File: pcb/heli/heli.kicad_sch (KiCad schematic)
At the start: 18 parts, among them J1 Batterie, J2 Debug, J3 Radio, Q1 IRLZ44N, SW1 SW_Push, U1 AZ1117-3.3, U2 STM32F103CBTx

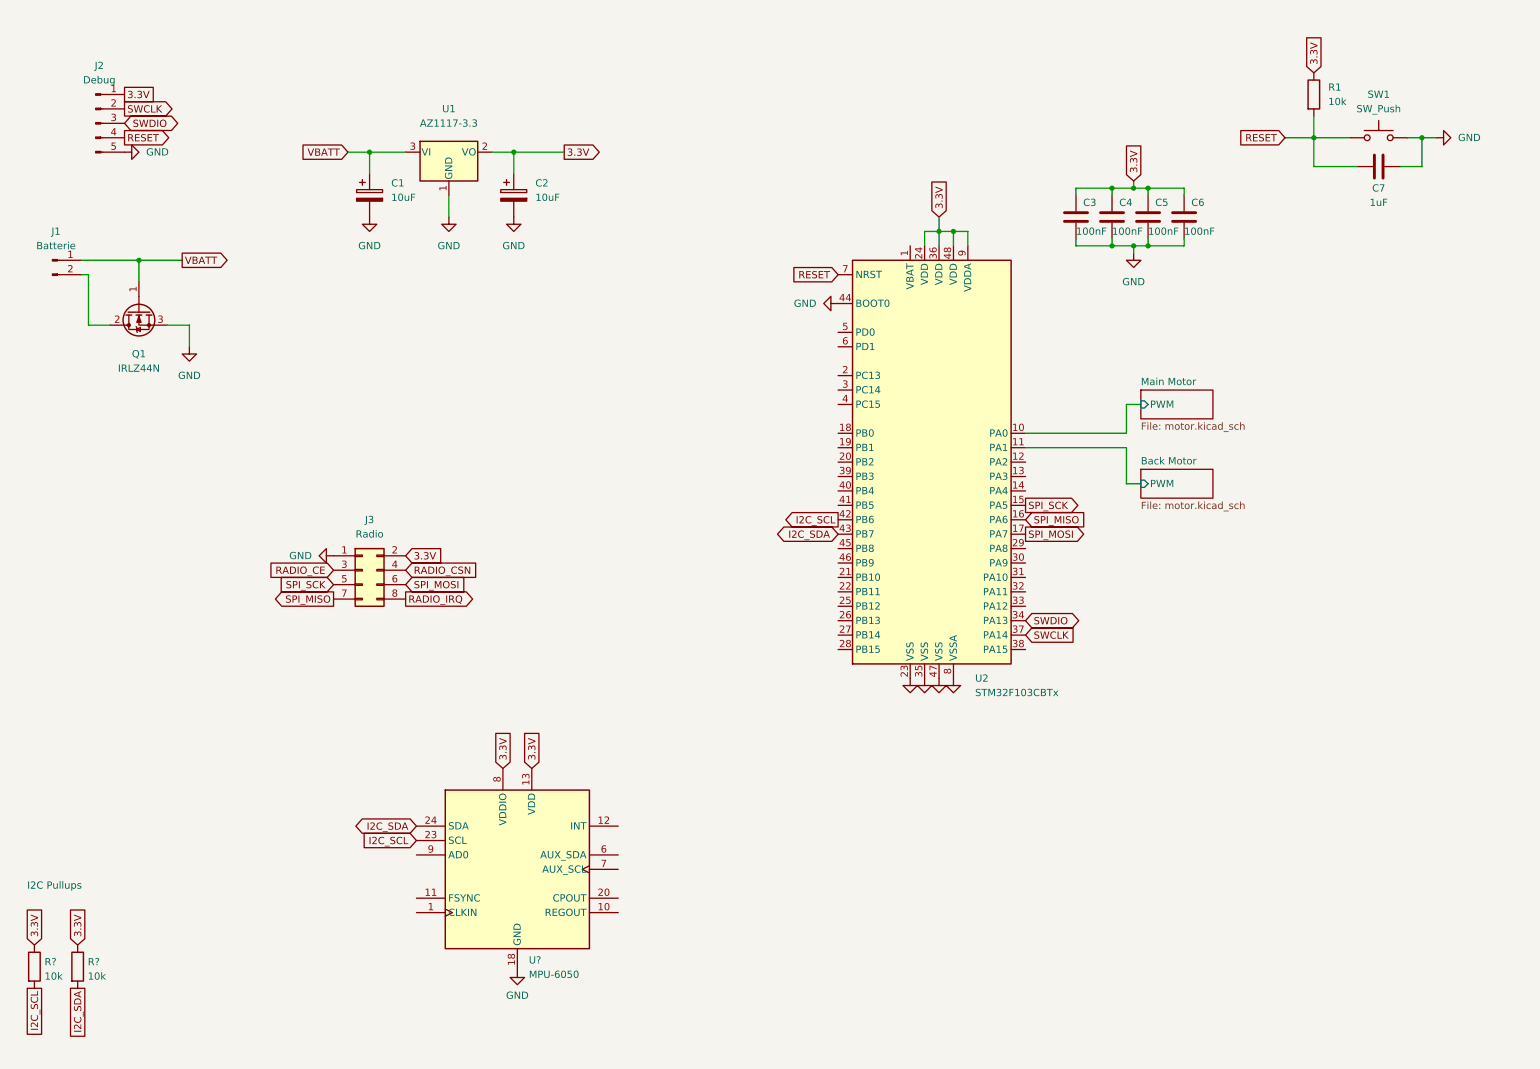
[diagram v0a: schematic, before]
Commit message: 
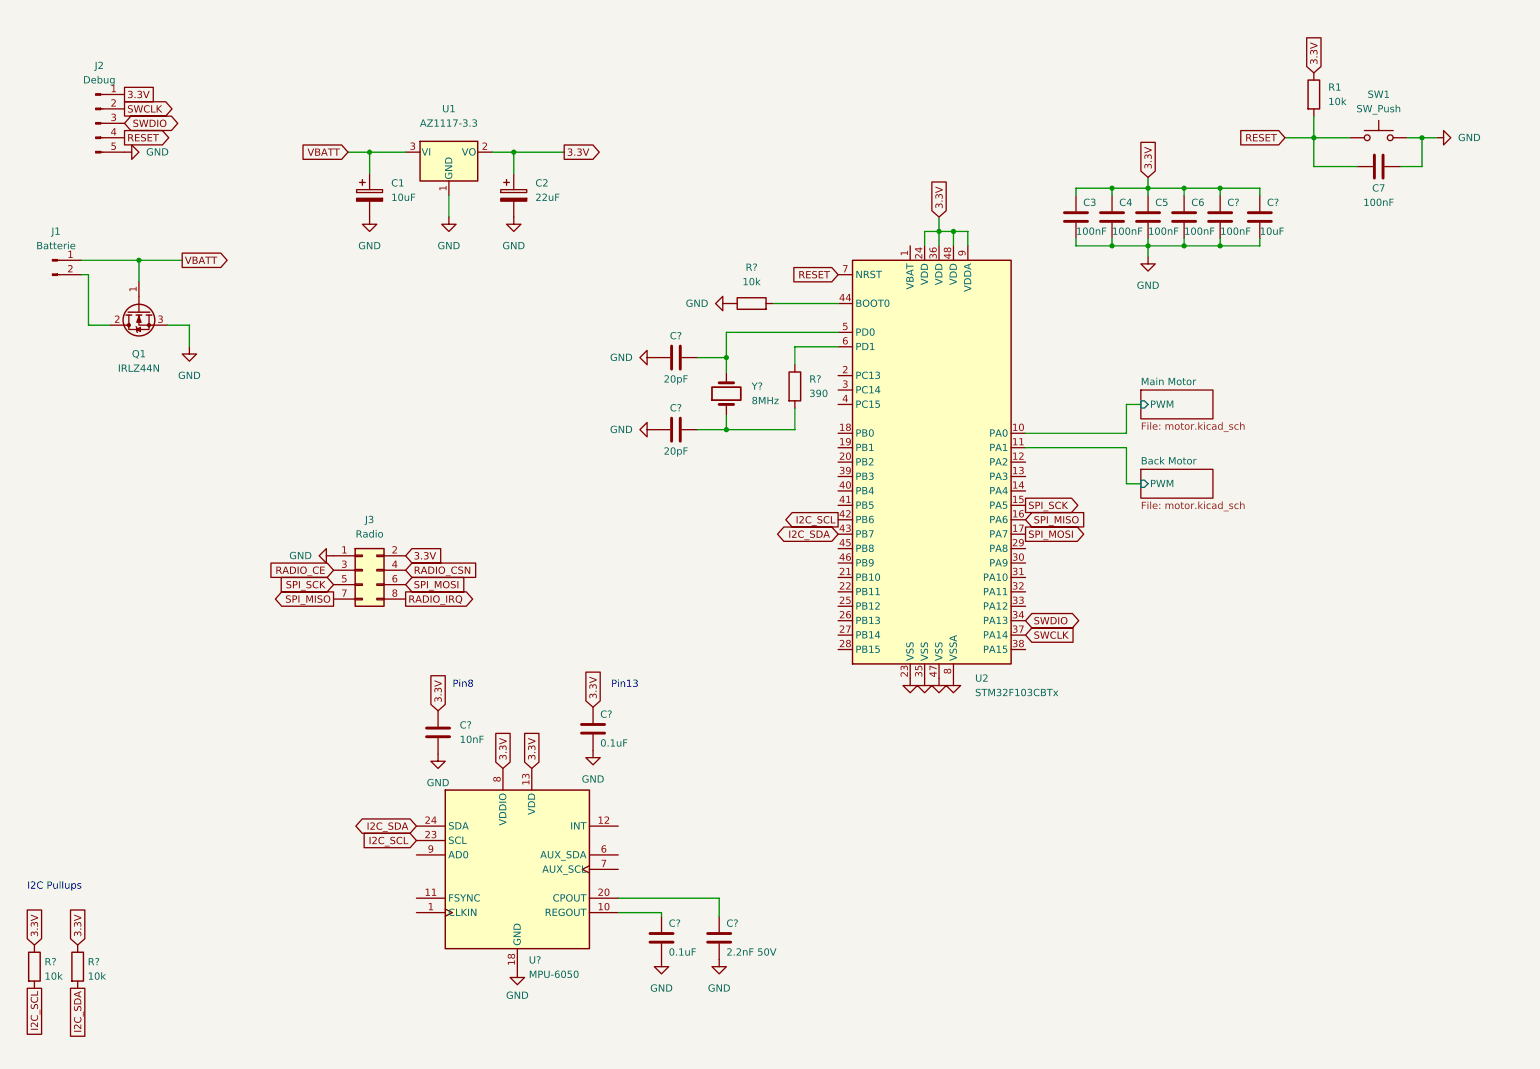
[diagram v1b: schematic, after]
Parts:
- added C? (x2): 20pF, symbol Device:C
- added C?: 2.2nF 50V, symbol Device:C
- added C? (x2): 0.1uF, symbol Device:C
- added C?: 100nF, symbol Device:C
- added C?: 10uF, symbol Device:C
- added C?: 10nF, symbol Device:C
- added R?: 10k, symbol Device:R
- added R?: 390, symbol Device:R
- added Y?: 8MHz, symbol Device:Crystal
- C2: value 10uF -> 22uF
- C7: value 1uF -> 100nF
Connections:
- net 3.3V: now also C?.1, C?.1, C?.1, C?.1
- net GND: now also C?.1, C?.1, C?.2, C?.2, C?.2, C?.2, C?.2, C?.2, R?.1; no longer U2.44 (BOOT0)
- net at U2.5 (PD0): now also C?.2, Y?.2
- net at U2.6 (PD1): now also R?.1
- net at U?.10 (REGOUT): now also C?.1
- net at U?.20 (CPOUT): now also C?.1
- new net: C?.2, R?.2, Y?.1
- new net: R?.2, U2.44 (BOOT0)
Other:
- note added: "Pin13"
- note added: "Pin8"

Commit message: 
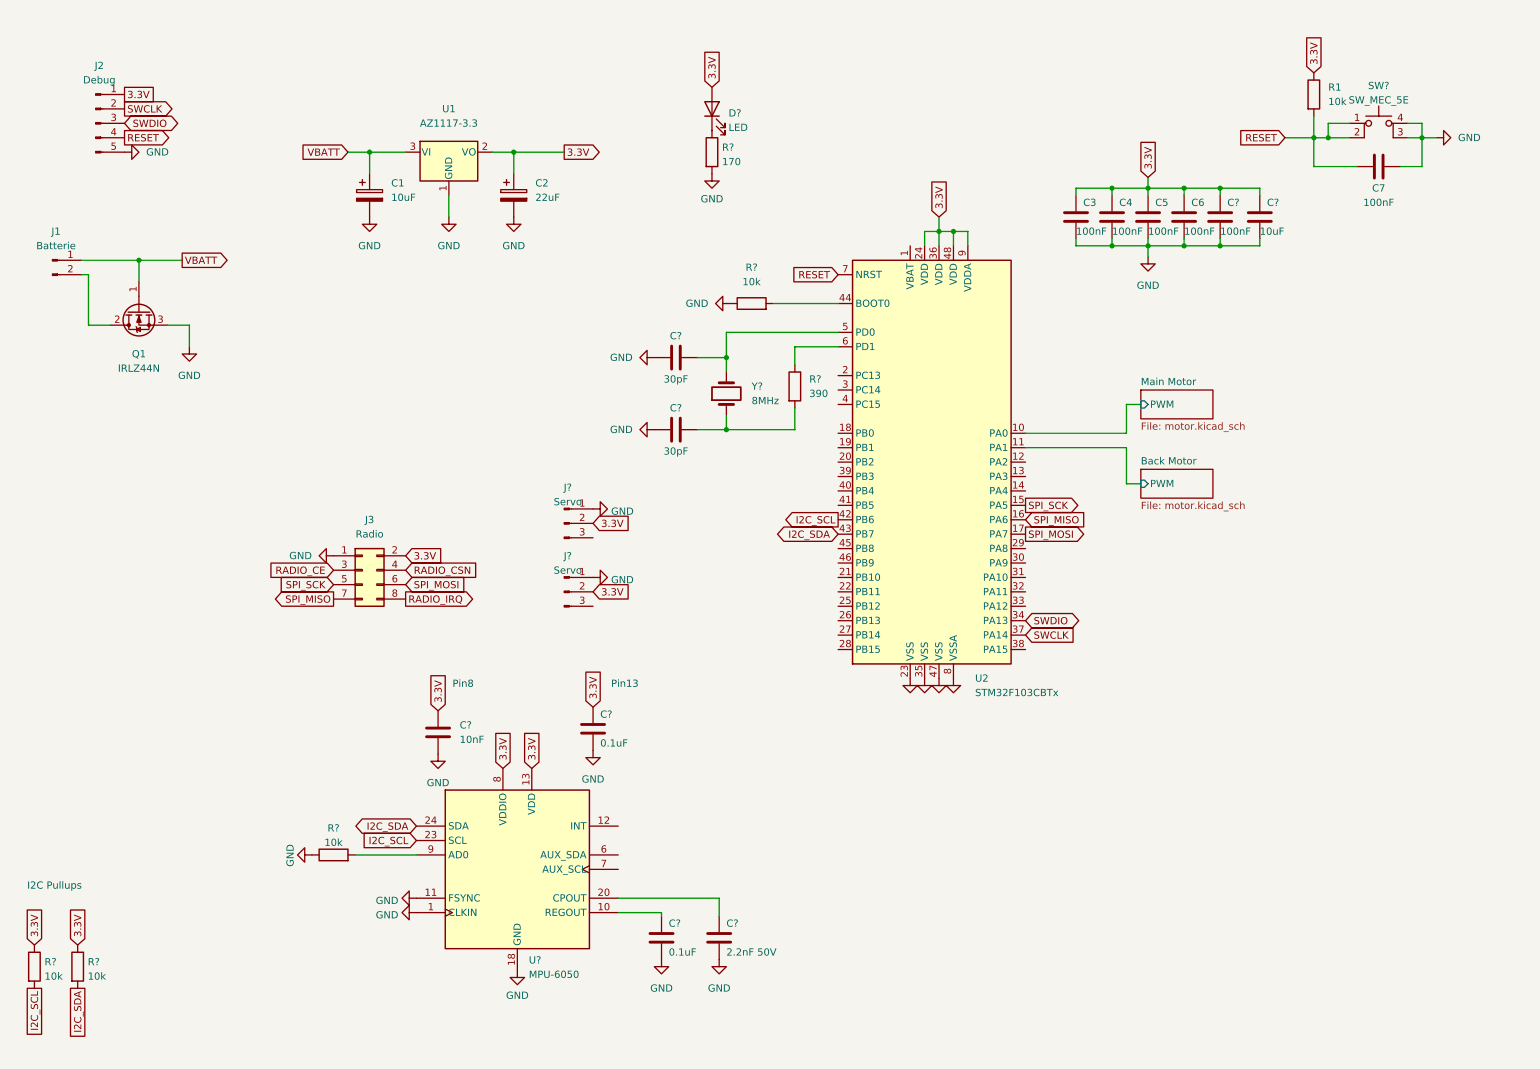
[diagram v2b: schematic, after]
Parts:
- removed SW1: SW_Push, symbol Switch:SW_Push
- added D?: LED, LED_SMD:LED_0603_1608Metric, symbol Device:LED
- added J? (x2): Servo, Connector_PinHeader_2.54mm:PinHeader_1x03_P2.54mm_Vertical, symbol Connector:Conn_01x03_Male
- added R?: 10k, Resistor_SMD:R_0603_1608Metric, symbol Device:R
- added R?: 170, Resistor_SMD:R_0603_1608Metric, symbol Device:R
- added SW?: SW_MEC_5E, Button_Switch_SMD:SW_SPST_TL3305A, symbol Switch:SW_MEC_5E
- C1, C2: footprint (none) -> Capacitor_SMD:CP_Elec_4x5.4
- C3, C4, C5, C6, C7, C? (x6): footprint (none) -> Capacitor_SMD:C_0603_1608Metric
- C? (x2): value 20pF -> 30pF; footprint (none) -> Capacitor_SMD:C_0603_1608Metric
- J1: footprint (none) -> Connector_PinHeader_2.54mm:PinHeader_1x02_P2.54mm_Horizontal
- J2: footprint (none) -> Connector_PinHeader_2.54mm:PinHeader_1x05_P2.54mm_Vertical
- J3: footprint (none) -> Connector_PinHeader_2.54mm:PinHeader_2x04_P2.54mm_Vertical
- R1, R? (x4): footprint (none) -> Resistor_SMD:R_0603_1608Metric
- U1: footprint (none) -> Package_TO_SOT_SMD:SOT-223-3_TabPin2
- Y?: footprint (none) -> Crystal:Crystal_HC49-4H_Vertical
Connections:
- net 3.3V: now also D?.2 (A), J?.2 (Pin_2), J?.2 (Pin_2)
- net GND: now also U?.1 (CLKIN), U?.11 (FSYNC), J?.1 (Pin_1), J?.1 (Pin_1), R?.1, R?.2, SW?.3 (K), SW?.4 (A)
- net RESET: now also SW?.1, SW?.2
- net at U?.9 (AD0): now also R?.2
- new net: D?.1 (K), R?.1
